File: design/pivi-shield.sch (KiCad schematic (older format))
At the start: 1 part

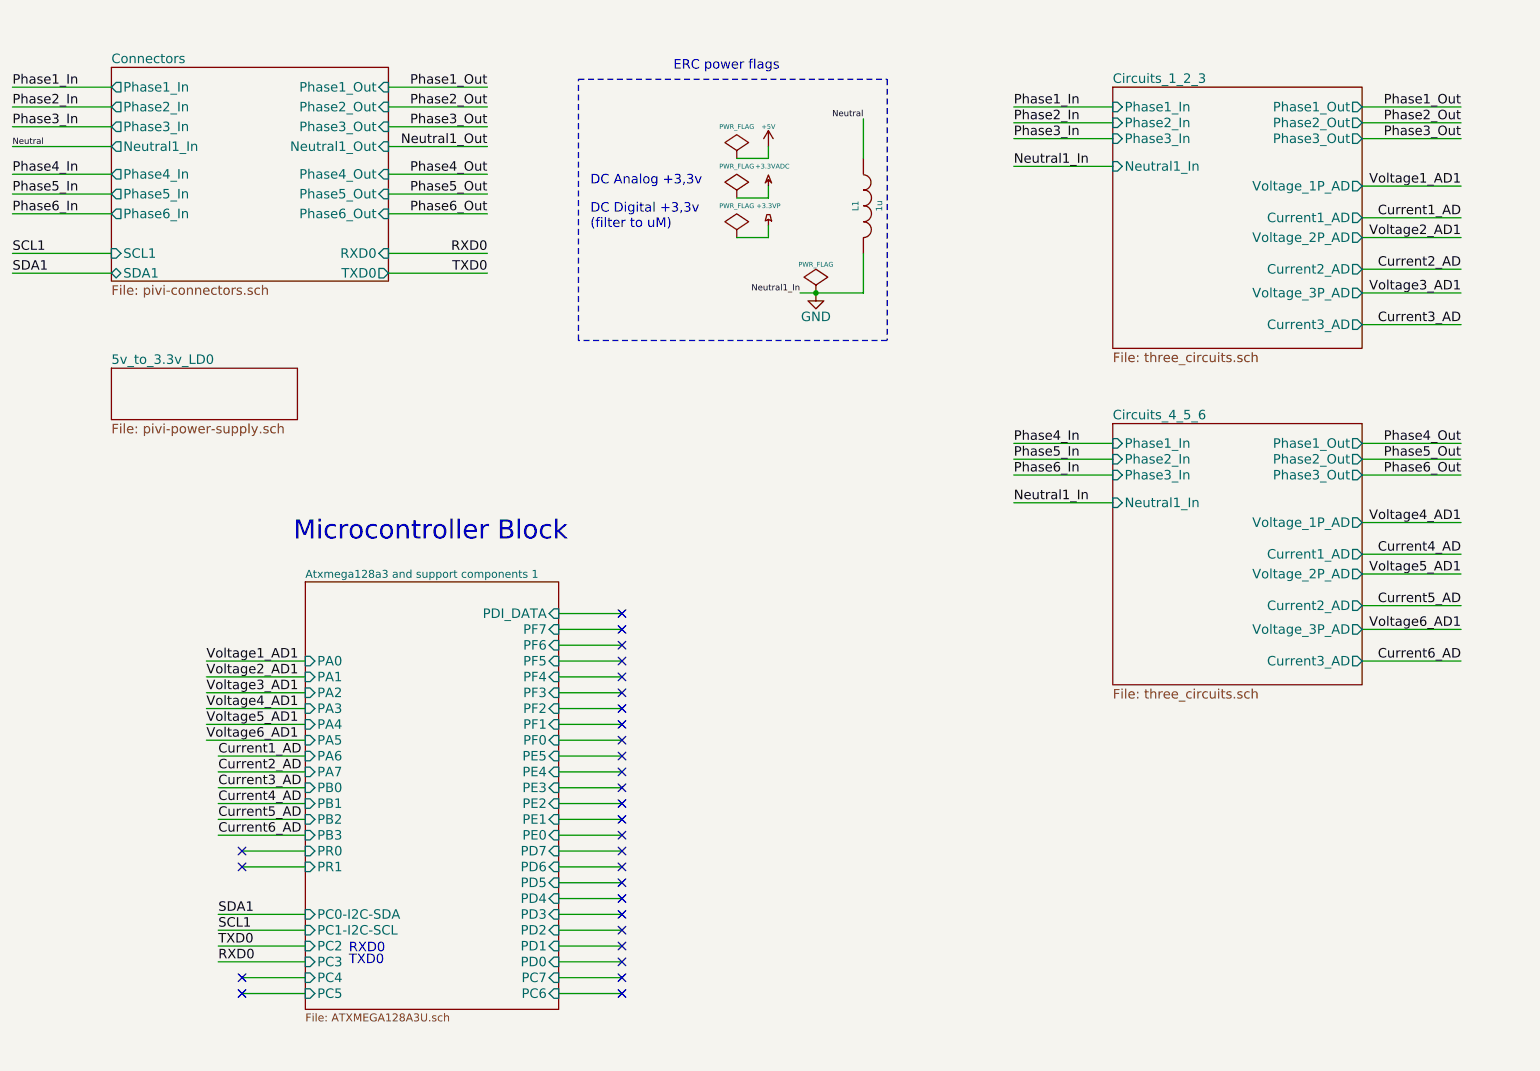
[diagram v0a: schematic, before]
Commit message: Moving to PIVI 2.0, added circuits for current clamps
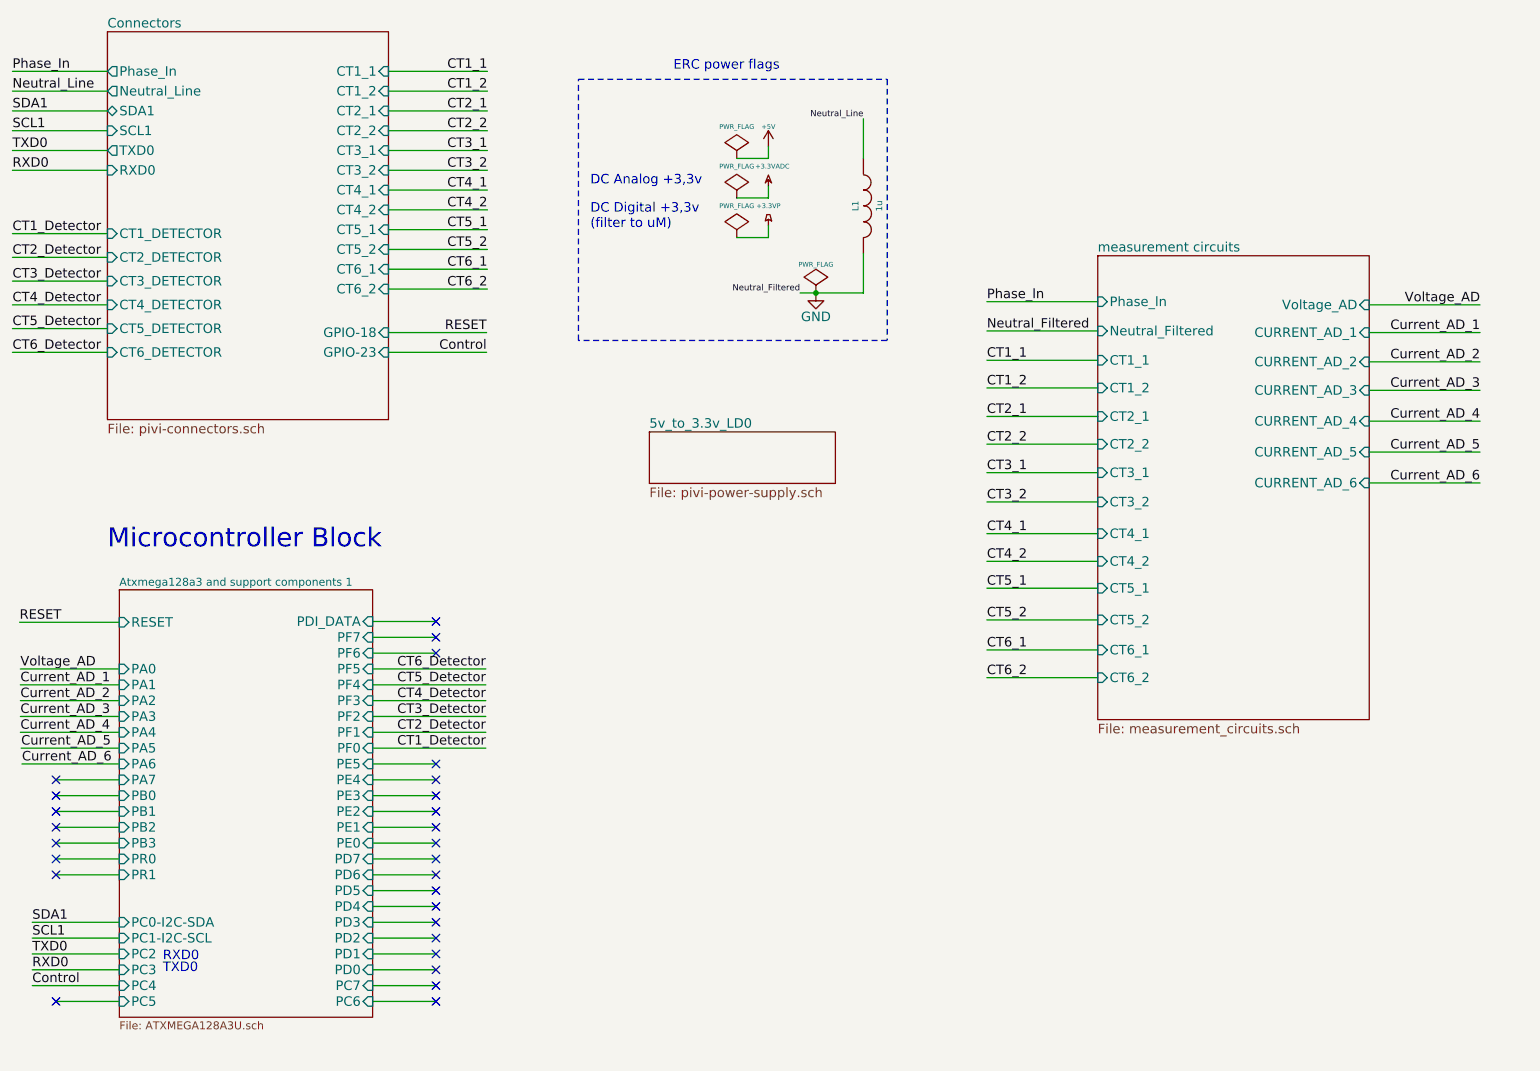
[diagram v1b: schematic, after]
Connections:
- net Neutral renamed Neutral_Line
- no-connect marks 29 -> 27

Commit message: Fixing connection errors
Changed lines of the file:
@@
 F0 "Connectors" 60
 F1 "pivi-connectors.sch" 60
-F2 "Phase_In" O L 1675 1200 60
-F3 "SDA1" B L 1675 1450 60
-F4 "SCL1" I L 1675 1575 60
-F5 "TXD0" O L 1675 1700 60
-F6 "RXD0" I L 1675 1825 60
-F7 "CT1_DETECTOR" I L 1675 2225 60
-F8 "CT1_1" I R 3450 1200 60
-F9 "CT1_2" I R 3450 1325 60
-F10 "CT2_DETECTOR" I L 1675 2375 60
-F11 "CT2_1" I R 3450 1450 60
-F12 "CT2_2" I R 3450 1575 60
-F13 "CT3_DETECTOR" I L 1675 2525 60
-F14 "CT3_1" I R 3450 1700 60
-F15 "CT3_2" I R 3450 1825 60
-F16 "CT4_DETECTOR" I L 1675 2675 60
-F17 "CT4_1" I R 3450 1950 60
-F18 "CT4_2" I R 3450 2075 60
-F19 "CT5_DETECTOR" I L 1675 2825 60
-F20 "CT5_1" I R 3450 2200 60
-F21 "CT5_2" I R 3450 2325 60
-F22 "CT6_DETECTOR" I L 1675 2975 60
-F23 "CT6_1" I R 3450 2450 60
-F24 "CT6_2" I R 3450 2575 60
-F25 "Neutral_Line" O L 1675 1325 60
-F26 "GPIO-18" I R 3450 2850 60
-F27 "GPIO-23" I R 3450 2975 60
+F2 "SDA1" B L 1675 1450 60
+F3 "SCL1" I L 1675 1575 60
+F4 "TXD0" O L 1675 1700 60
+F5 "RXD0" I L 1675 1825 60
+F6 "CT1_DETECTOR" I L 1675 2225 60
+F7 "CT1_1" I R 3450 1200 60
+F8 "CT1_2" I R 3450 1325 60
+F9 "CT2_DETECTOR" I L 1675 2375 60
+F10 "CT2_1" I R 3450 1450 60
+F11 "CT2_2" I R 3450 1575 60
+F12 "CT3_DETECTOR" I L 1675 2525 60
+F13 "CT3_1" I R 3450 1700 60
+F14 "CT3_2" I R 3450 1825 60
+F15 "CT4_DETECTOR" I L 1675 2675 60
+F16 "CT4_1" I R 3450 1950 60
+F17 "CT4_2" I R 3450 2075 60
+F18 "CT5_DETECTOR" I L 1675 2825 60
+F19 "CT5_1" I R 3450 2200 60
+F20 "CT5_2" I R 3450 2325 60
+F21 "CT6_DETECTOR" I L 1675 2975 60
+F22 "CT6_1" I R 3450 2450 60
+F23 "CT6_2" I R 3450 2575 60
+F24 "Neutral_Line" O L 1675 1325 60
+F25 "GPIO-18" I R 3450 2850 60
+F26 "GPIO-23" I R 3450 2975 60
+F27 "Phase_Line" O L 1675 1200 60
 $EndSheet
 $Sheet
@@
 F0 "measurement circuits" 60
 F1 "measurement_circuits.sch" 60
-F2 "Phase_ln" I L 7930 2655 60
-F3 "CT1_1" I L 7930 3025 60
-F4 "CT1_2" I L 7930 3200 60
-F5 "CURRENT_AD_1" I R 9645 2850 60
-F6 "CT2_1" I L 7930 3380 60
-F7 "CT2_2" I L 7930 3555 60
-F8 "CT3_1" I L 7930 3735 60
-F9 "CT3_2" I L 7930 3920 60
-F10 "CT4_1" I L 7930 4120 60
-F11 "CT4_2" I L 7930 4295 60
-F12 "CT5_1" I L 7930 4465 60
-F13 "CT5_2" I L 7930 4665 60
-F14 "CT6_1" I L 7930 4855 60
-F15 "CT6_2" I L 7930 5030 60
-F16 "CURRENT_AD_2" I R 9645 3035 60
-F17 "CURRENT_AD_3" I R 9645 3215 60
-F18 "CURRENT_AD_4" I R 9645 3410 60
-F19 "CURRENT_AD_5" I R 9645 3605 60
-F20 "CURRENT_AD_6" I R 9645 3800 60
-F21 "Voltage_AD" I R 9645 2675 60
-F22 "Neutral_Filtered" I L 7930 2840 60
+F2 "CT1_1" I L 7930 3025 60
+F3 "CT1_2" I L 7930 3200 60
+F4 "CURRENT_AD_1" I R 9645 2850 60
+F5 "CT2_1" I L 7930 3380 60
+F6 "CT2_2" I L 7930 3555 60
+F7 "CT3_1" I L 7930 3735 60
+F8 "CT3_2" I L 7930 3920 60
+F9 "CT4_1" I L 7930 4120 60
+F10 "CT4_2" I L 7930 4295 60
+F11 "CT5_1" I L 7930 4465 60
+F12 "CT5_2" I L 7930 4665 60
+F13 "CT6_1" I L 7930 4855 60
+F14 "CT6_2" I L 7930 5030 60
+F15 "CURRENT_AD_2" I R 9645 3035 60
+F16 "CURRENT_AD_3" I R 9645 3215 60
+F17 "CURRENT_AD_4" I R 9645 3410 60
+F18 "CURRENT_AD_5" I R 9645 3605 60
+F19 "CURRENT_AD_6" I R 9645 3800 60
+F20 "Voltage_AD" I R 9645 2675 60
+F21 "Neutral_Filtered" I L 7930 2840 60
+F22 "Phase_Line" I L 7930 2655 60
 $EndSheet
 Text Label 1125 5075 0    60   ~ 0
@@
 NoConn ~ 1350 5675
 Text Label 1075 1200 0    60   ~ 0
-Phase_In
+Phase_Line
 Wire Wire Line
 	1350 7075 1750 7075
@@
 CT6_2
 Text Label 7230 2655 0    60   ~ 0
-Phase_ln
+Phase_Line
 Text Label 7230 2840 0    59   ~ 0
 Neutral_Filtered

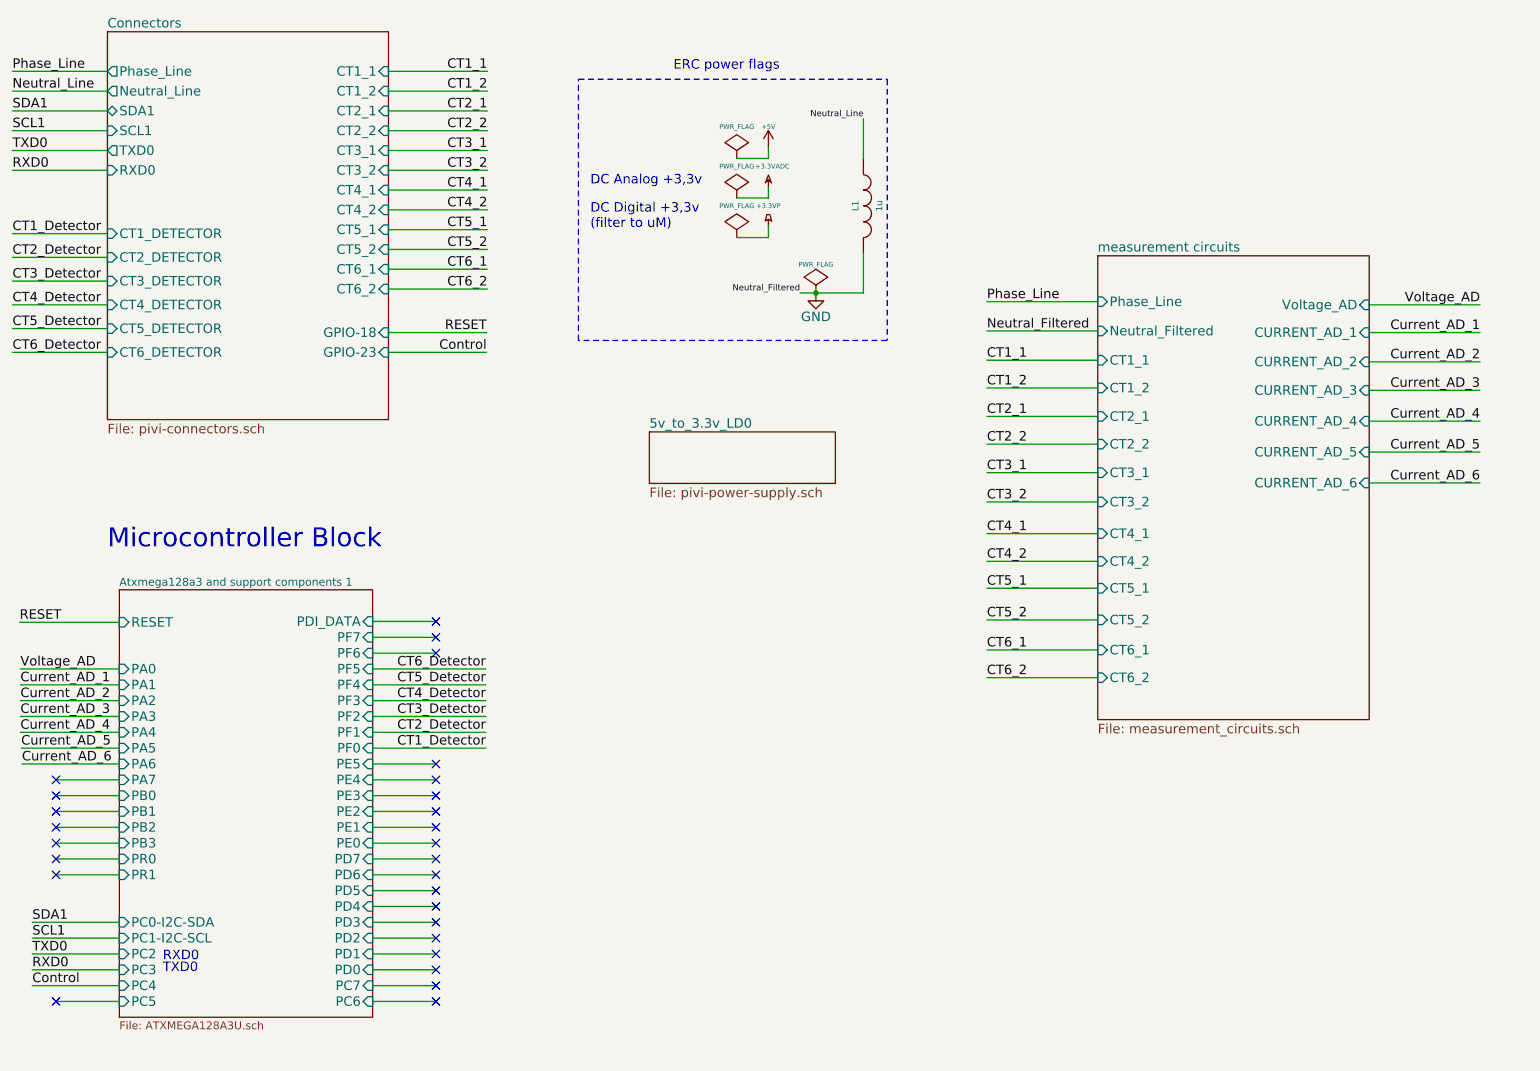
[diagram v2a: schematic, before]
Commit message: Agrego los dos circuitos extra para medir tension
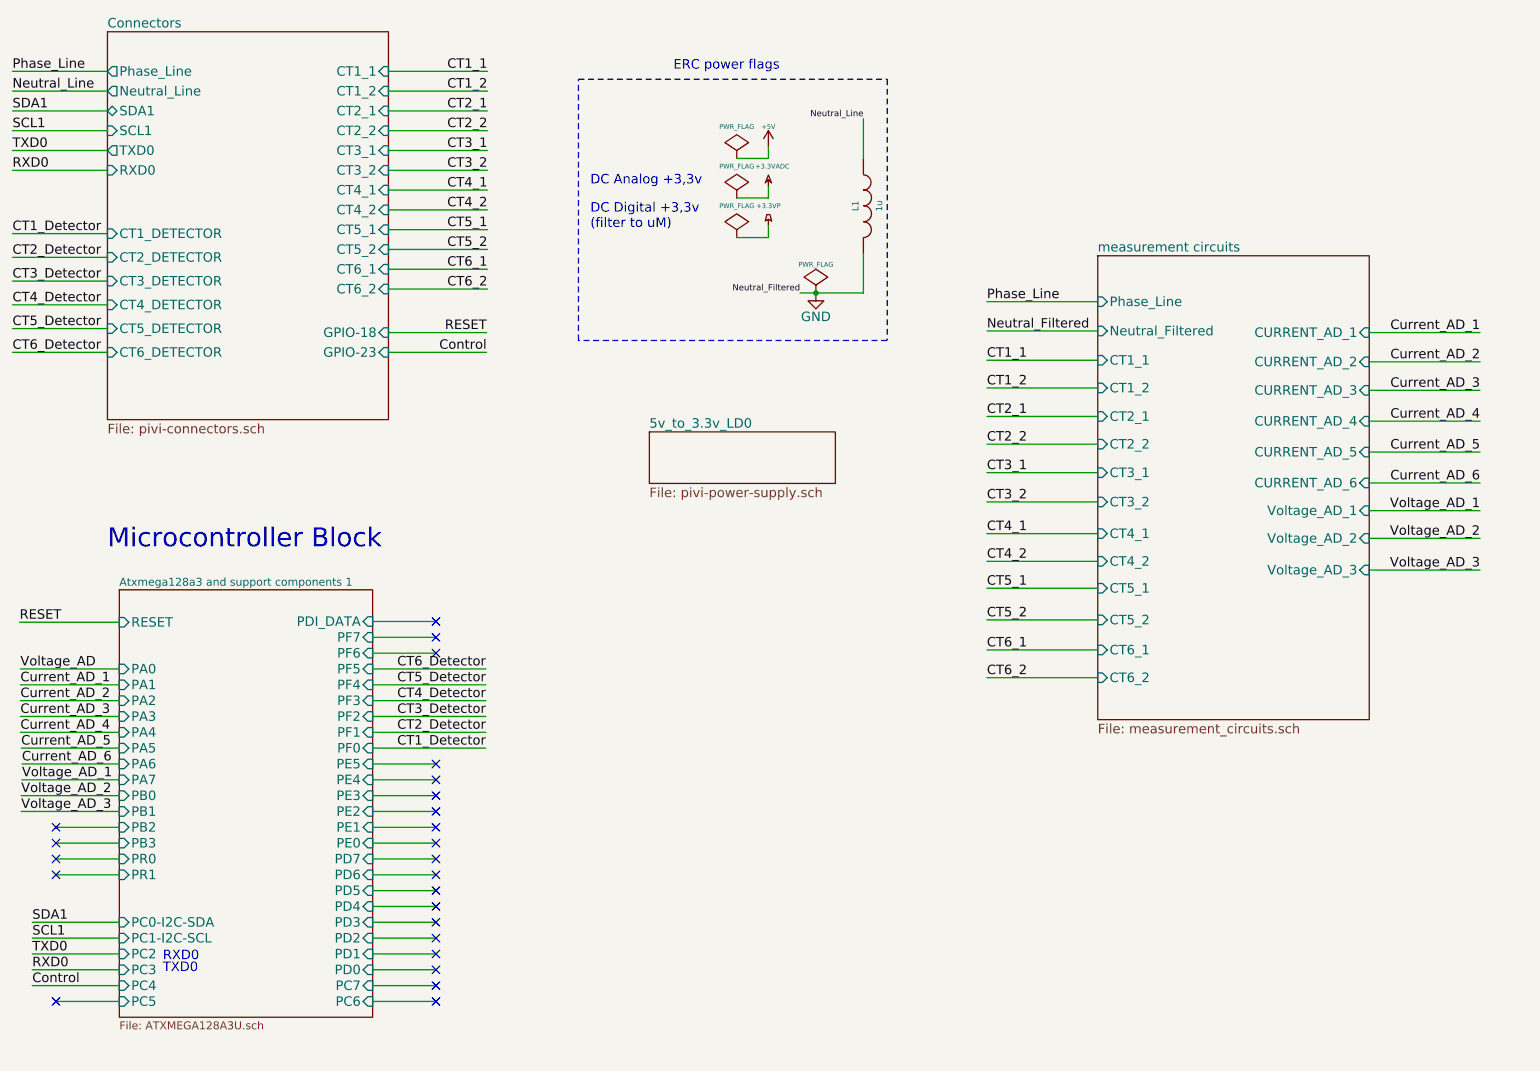
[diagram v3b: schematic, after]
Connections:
- no-connect marks 27 -> 24
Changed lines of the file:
@@
 LIBS:memory
 LIBS:xilinx
-LIBS:special
 LIBS:microcontrollers
 LIBS:dsp
@@
 $Descr A4 11693 8268
 encoding utf-8
-Sheet 1 18
+Sheet 1 20
 Title "PIVI"
 Date "Mon 27 Jul 2015"
@@
 F18 "CURRENT_AD_5" I R 9645 3605 60
 F19 "CURRENT_AD_6" I R 9645 3800 60
-F20 "Voltage_AD" I R 9645 2675 60
-F21 "Neutral_Filtered" I L 7930 2840 60
-F22 "Phase_Line" I L 7930 2655 60
+F20 "Neutral_Filtered" I L 7930 2840 60
+F21 "Phase_Line" I L 7930 2655 60
+F22 "Voltage_AD_1" I R 9645 3975 60
+F23 "Voltage_AD_2" I R 9645 4150 60
+F24 "Voltage_AD_3" I R 9645 4350 60
 $EndSheet
 Text Label 1125 5075 0    60   ~ 0
@@
 NoConn ~ 1350 6075
 NoConn ~ 1350 5975
-NoConn ~ 1350 5875
-NoConn ~ 1350 5775
-NoConn ~ 1350 5675
 Text Label 1075 1200 0    60   ~ 0
 Phase_Line
@@
 	1350 5975 1750 5975
 Wire Wire Line
-	1350 5875 1750 5875
-Wire Wire Line
-	1350 5775 1750 5775
-Wire Wire Line
-	1350 5675 1750 5675
+	1130 5875 1750 5875
+Wire Wire Line
+	1135 5675 1750 5675
 Wire Wire Line
 	3450 1200 4075 1200
@@
 Wire Wire Line
 	1675 2975 1075 2975
-Text Label 10345 2675 2    60   ~ 0
-Voltage_AD
-Wire Wire Line
-	9645 2675 10345 2675
+Text Label 10345 3975 2    60   ~ 0
+Voltage_AD_1
+Wire Wire Line
+	9645 3975 10345 3975
 Wire Wire Line
 	9645 2850 10345 2850
@@
 Text Label 4070 2850 2    60   ~ 0
 RESET
+Text Label 10345 4150 2    60   ~ 0
+Voltage_AD_2
+Wire Wire Line
+	9645 4150 10345 4150
+Text Label 10345 4350 2    60   ~ 0
+Voltage_AD_3
+Wire Wire Line
+	9645 4350 10345 4350
+Text Label 1135 5675 0    60   ~ 0
+Voltage_AD_1
+Text Label 1130 5775 0    60   ~ 0
+Voltage_AD_2
+Text Label 1130 5875 0    60   ~ 0
+Voltage_AD_3
+Wire Wire Line
+	1750 5775 1130 5775
 $EndSCHEMATC

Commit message: Edito conexiones pinza, agregado debub uart, agregado tension referencia
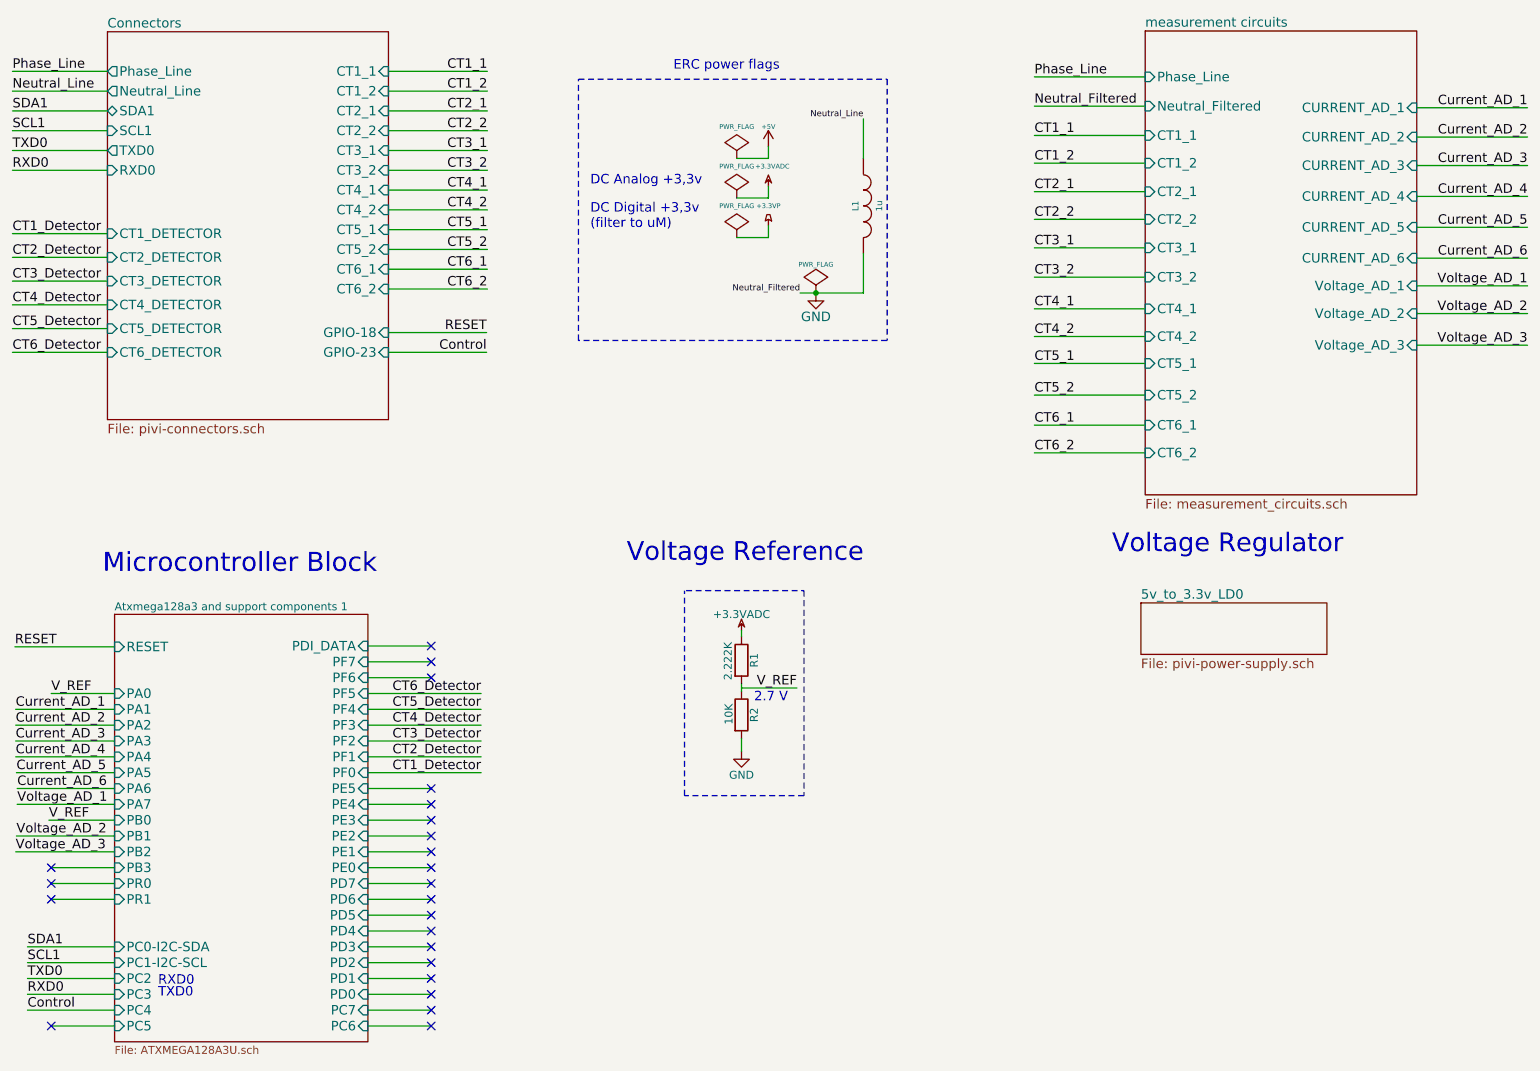
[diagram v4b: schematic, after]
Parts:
- added R1: 2.222K, symbol R
- added R2: 10K, symbol R
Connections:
- net +3.3VADC: now also R1.1
- net GND: now also R2.2
- new net: R1.2, R2.1
- no-connect marks 24 -> 23
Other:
- note added: "2.7 V"
- note added: "Voltage Reference\n"
- note added: "Voltage Regulator"
